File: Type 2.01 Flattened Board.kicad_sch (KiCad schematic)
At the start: 8 parts, among them U10 74AHC125

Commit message: Redo pinout to simplify routing
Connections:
- net BUS.PA2: no longer XA2.A0
- net BUS.PA4: no longer XA2.D2 (D2_INT0)
- net BUS.PA5: no longer XA2.A1
- net BUS.PA6: no longer XA2.D3 (D3_INT1)
- net BUS.PA7: no longer XA2.D4
- net BUS.PB3: no longer XA2.A2
- net BUS.PB4: no longer XA2.A3
- net BUS.PB5: no longer XA2.A4
- net BUS.PB6: no longer XA2.A5
- net BUS.PB7: no longer XA2.D5
- net BUS.PB8: no longer XA2.D6
- net BUS.PB9: no longer XA2.D7
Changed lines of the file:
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@@
     (company "Joshua Scoggins")
   )
+  (bus_alias "CCL" (members "IN[0..11]" "OUT[0..3]"))
   (bus_alias "MetroM4" (members "D[0..13]" "SCL" "SDA" "AREF" "A[0..5]" "MISO" "MOSI" "SCK" "~{RESET[0..1]}" "VIN"))
-  (bus_alias "CCL" (members "IN[0..11]" "OUT[0..3]"))
   (junction (at 54.102 162.052) (diameter 0) (color 0 0 0 0)
   )
@@
     (stroke (width 0) (type default) (color 0 0 0 0))
   )
+  (bus_entry (at 251.46 86.36) (size 2.54 2.54)
+    (stroke (width 0) (type default) (color 0 0 0 0))
+  )
+  (bus_entry (at 248.92 86.36) (size 2.54 2.54)
+    (stroke (width 0) (type default) (color 0 0 0 0))
+  )
   (bus_entry (at 23.368 141.732) (size 2.54 2.54)
     (stroke (width 0) (type default) (color 0 0 0 0))
@@
     (stroke (width 0) (type default) (color 0 0 0 0))
   )
+  (bus (pts (xy 248.92 86.36) (xy 251.46 86.36))
+    (stroke (width 0) (type default) (color 0 0 0 0))
+  )
   (wire (pts (xy 312.039 38.1) (xy 347.345 38.1))
     (stroke (width 0) (type default) (color 0 0 0 0))
@@
     (stroke (width 0) (type default) (color 0 0 0 0))
   )
-  (bus (pts (xy 246.38 86.36) (xy 309.499 86.36))
+  (bus (pts (xy 246.38 86.36) (xy 248.92 86.36))
     (stroke (width 0) (type default) (color 0 0 0 0))
   )
@@
     (stroke (width 0) (type default) (color 0 0 0 0))
   )
+  (bus (pts (xy 251.46 86.36) (xy 309.499 86.36))
+    (stroke (width 0) (type default) (color 0 0 0 0))
+  )
   (wire (pts (xy 139.7 108.712) (xy 187.452 108.712))
     (stroke (width 0) (type default) (color 0 0 0 0))
@@
     (stroke (width 0) (type default) (color 0 0 0 0))
   )
+  (wire (pts (xy 254 88.9) (xy 254 102.87))
+    (stroke (width 0) (type default) (color 0 0 0 0))
+  )
   (wire (pts (xy 256.54 184.785) (xy 271.145 184.785))
     (stroke (width 0) (type default) (color 0 0 0 0))
@@
   )
   (bus (pts (xy 238.76 86.36) (xy 241.3 86.36))
+    (stroke (width 0) (type default) (color 0 0 0 0))
+  )
+  (wire (pts (xy 251.46 88.9) (xy 251.46 102.87))
     (stroke (width 0) (type default) (color 0 0 0 0))
   )
@@
     (effects (font (size 1.27 1.27)) (justify right bottom))
   )
-  (label "BUS.PC18" (at 347.345 73.66 180)
+  (label "BUS.PC18" (at 359.41 90.17 180)
     (effects (font (size 1.27 1.27)) (justify right bottom))
   )
@@
     (effects (font (size 1.27 1.27)) (justify left bottom))
   )
-  (label "BUS.PB8" (at 189.484 226.822 180)
+  (label "BUS.PB8" (at 347.345 76.2 180)
     (effects (font (size 1.27 1.27)) (justify right bottom))
   )
@@
     (effects (font (size 1.27 1.27)) (justify left bottom))
   )
-  (label "BUS.PB4" (at 34.544 239.522 0)
-    (effects (font (size 1.27 1.27)) (justify left bottom))
+  (label "BUS.PB4" (at 347.345 68.58 180)
+    (effects (font (size 1.27 1.27)) (justify right bottom))
   )
   (label "BUS.PC15" (at 145.288 154.432 0)
     (effects (font (size 1.27 1.27)) (justify left bottom))
   )
-  (label "BUS.PA4" (at 189.484 216.662 180)
+  (label "BUS.PA4" (at 347.345 73.66 180)
     (effects (font (size 1.27 1.27)) (justify right bottom))
   )
@@
     (effects (font (size 1.27 1.27)) (justify right bottom))
   )
-  (label "BUS.PD21" (at 347.345 86.36 180)
+  (label "BUS.PD21" (at 384.81 70.485 180)
     (effects (font (size 1.27 1.27)) (justify right bottom))
   )
@@
     (effects (font (size 1.27 1.27)) (justify right bottom))
   )
-  (label "BUS.PB23" (at 347.345 66.04 180)
+  (label "BUS.PB23" (at 365.76 74.93 180)
     (effects (font (size 1.27 1.27)) (justify right bottom))
   )
@@
     (effects (font (size 1.27 1.27)) (justify right bottom))
   )
-  (label "BUS.PC21" (at 347.345 81.28 180)
+  (label "BUS.PC21" (at 389.89 86.36 180)
     (effects (font (size 1.27 1.27)) (justify right bottom))
   )
@@
     (effects (font (size 1.27 1.27)) (justify left bottom))
   )
-  (label "BUS.PB22" (at 347.345 63.5 180)
+  (label "BUS.PB22" (at 381.635 57.15 180)
     (effects (font (size 1.27 1.27)) (justify right bottom))
   )
@@
     (effects (font (size 1.27 1.27)) (justify left bottom))
   )
-  (label "BUS.PB2" (at 347.345 68.58 180)
-    (effects (font (size 1.27 1.27)) (justify right bottom))
-  )
-  (label "BUS.PA2" (at 34.544 247.142 0)
-    (effects (font (size 1.27 1.27)) (justify left bottom))
+  (label "BUS.PB2" (at 359.41 85.09 180)
+    (effects (font (size 1.27 1.27)) (justify right bottom))
+  )
+  (label "BUS.PA2" (at 251.46 89.535 270)
+    (effects (font (size 1.27 1.27)) (justify right bottom))
   )
   (label "GCM4.D11" (at 312.547 134.62 0)
@@
     (effects (font (size 1.27 1.27)) (justify left bottom))
   )
-  (label "BUS.PB3" (at 34.544 242.062 0)
-    (effects (font (size 1.27 1.27)) (justify left bottom))
+  (label "BUS.PB3" (at 347.345 86.36 180)
+    (effects (font (size 1.27 1.27)) (justify right bottom))
   )
   (label "~{RESET_{0}}" (at 189.484 267.462 180)
     (effects (font (size 1.27 1.27)) (justify right bottom))
   )
-  (label "BUS.PA6" (at 189.484 219.202 180)
+  (label "BUS.PA6" (at 347.345 81.28 180)
     (effects (font (size 1.27 1.27)) (justify right bottom))
   )
@@
     (effects (font (size 1.27 1.27)) (justify left bottom))
   )
-  (label "BUS.PB6" (at 34.544 234.442 0)
-    (effects (font (size 1.27 1.27)) (justify left bottom))
+  (label "BUS.PB6" (at 347.345 63.5 180)
+    (effects (font (size 1.27 1.27)) (justify right bottom))
   )
   (label "SPI_MOSI" (at 102.87 42.164 270)
@@
     (effects (font (size 1.27 1.27)) (justify left bottom))
   )
-  (label "BUS.PD20" (at 347.345 83.82 180)
+  (label "BUS.PD20" (at 384.81 67.945 180)
     (effects (font (size 1.27 1.27)) (justify right bottom))
   )
@@
     (effects (font (size 1.27 1.27)) (justify left bottom))
   )
-  (label "BUS.PB7" (at 189.484 224.282 180)
+  (label "BUS.PB7" (at 347.345 66.04 180)
     (effects (font (size 1.27 1.27)) (justify right bottom))
   )
@@
     (effects (font (size 1.27 1.27)) (justify left bottom))
   )
-  (label "BUS.PA7" (at 189.484 221.742 180)
+  (label "BUS.PA7" (at 347.345 83.82 180)
     (effects (font (size 1.27 1.27)) (justify right bottom))
   )
@@
     (effects (font (size 1.27 1.27)) (justify right bottom))
   )
+  (label "GCM4.~{BE1}" (at 254 102.87 270)
+    (effects (font (size 1.27 1.27)) (justify right bottom))
+  )
   (label "BUS.PA7" (at 61.214 144.272 0)
     (effects (font (size 1.27 1.27)) (justify left bottom))
@@
     (effects (font (size 1.27 1.27)) (justify left bottom))
   )
-  (label "BUS.PB5" (at 34.544 236.982 0)
-    (effects (font (size 1.27 1.27)) (justify left bottom))
+  (label "BUS.PB5" (at 347.345 71.12 180)
+    (effects (font (size 1.27 1.27)) (justify right bottom))
   )
   (label "GCM4.D7" (at 312.547 124.46 0)
     (effects (font (size 1.27 1.27)) (justify left bottom))
   )
-  (label "BUS.PB18" (at 347.345 71.12 180)
+  (label "BUS.PB18" (at 375.285 86.995 180)
     (effects (font (size 1.27 1.27)) (justify right bottom))
   )
@@
     (effects (font (size 1.27 1.27)) (justify left bottom))
   )
-  (label "BUS.PB9" (at 189.484 229.362 180)
+  (label "BUS.PB9" (at 347.345 78.74 180)
     (effects (font (size 1.27 1.27)) (justify right bottom))
   )
@@
     (effects (font (size 1.27 1.27)) (justify right bottom))
   )
-  (label "BUS.PC19" (at 347.345 76.2 180)
+  (label "BUS.PC19" (at 384.175 79.375 180)
     (effects (font (size 1.27 1.27)) (justify right bottom))
   )
@@
     (effects (font (size 1.27 1.27)) (justify left bottom))
   )
-  (label "BUS.PA5" (at 34.544 244.602 0)
-    (effects (font (size 1.27 1.27)) (justify left bottom))
+  (label "BUS.PA5" (at 254 89.535 270)
+    (effects (font (size 1.27 1.27)) (justify right bottom))
   )
   (label "BUS.PC17" (at 347.345 129.54 180)
     (effects (font (size 1.27 1.27)) (justify right bottom))
   )
-  (label "BUS.PC20" (at 347.345 78.74 180)
-    (effects (font (size 1.27 1.27)) (justify right bottom))
-  )
+  (label "GCM4.~{BE0}" (at 251.46 102.87 270)
+    (effects (font (size 1.27 1.27)) (justify right bottom))
+  )
+  (label "BUS.PC20" (at 363.855 80.01 180)
+    (effects (font (size 1.27 1.27)) (justify right bottom))
+  )

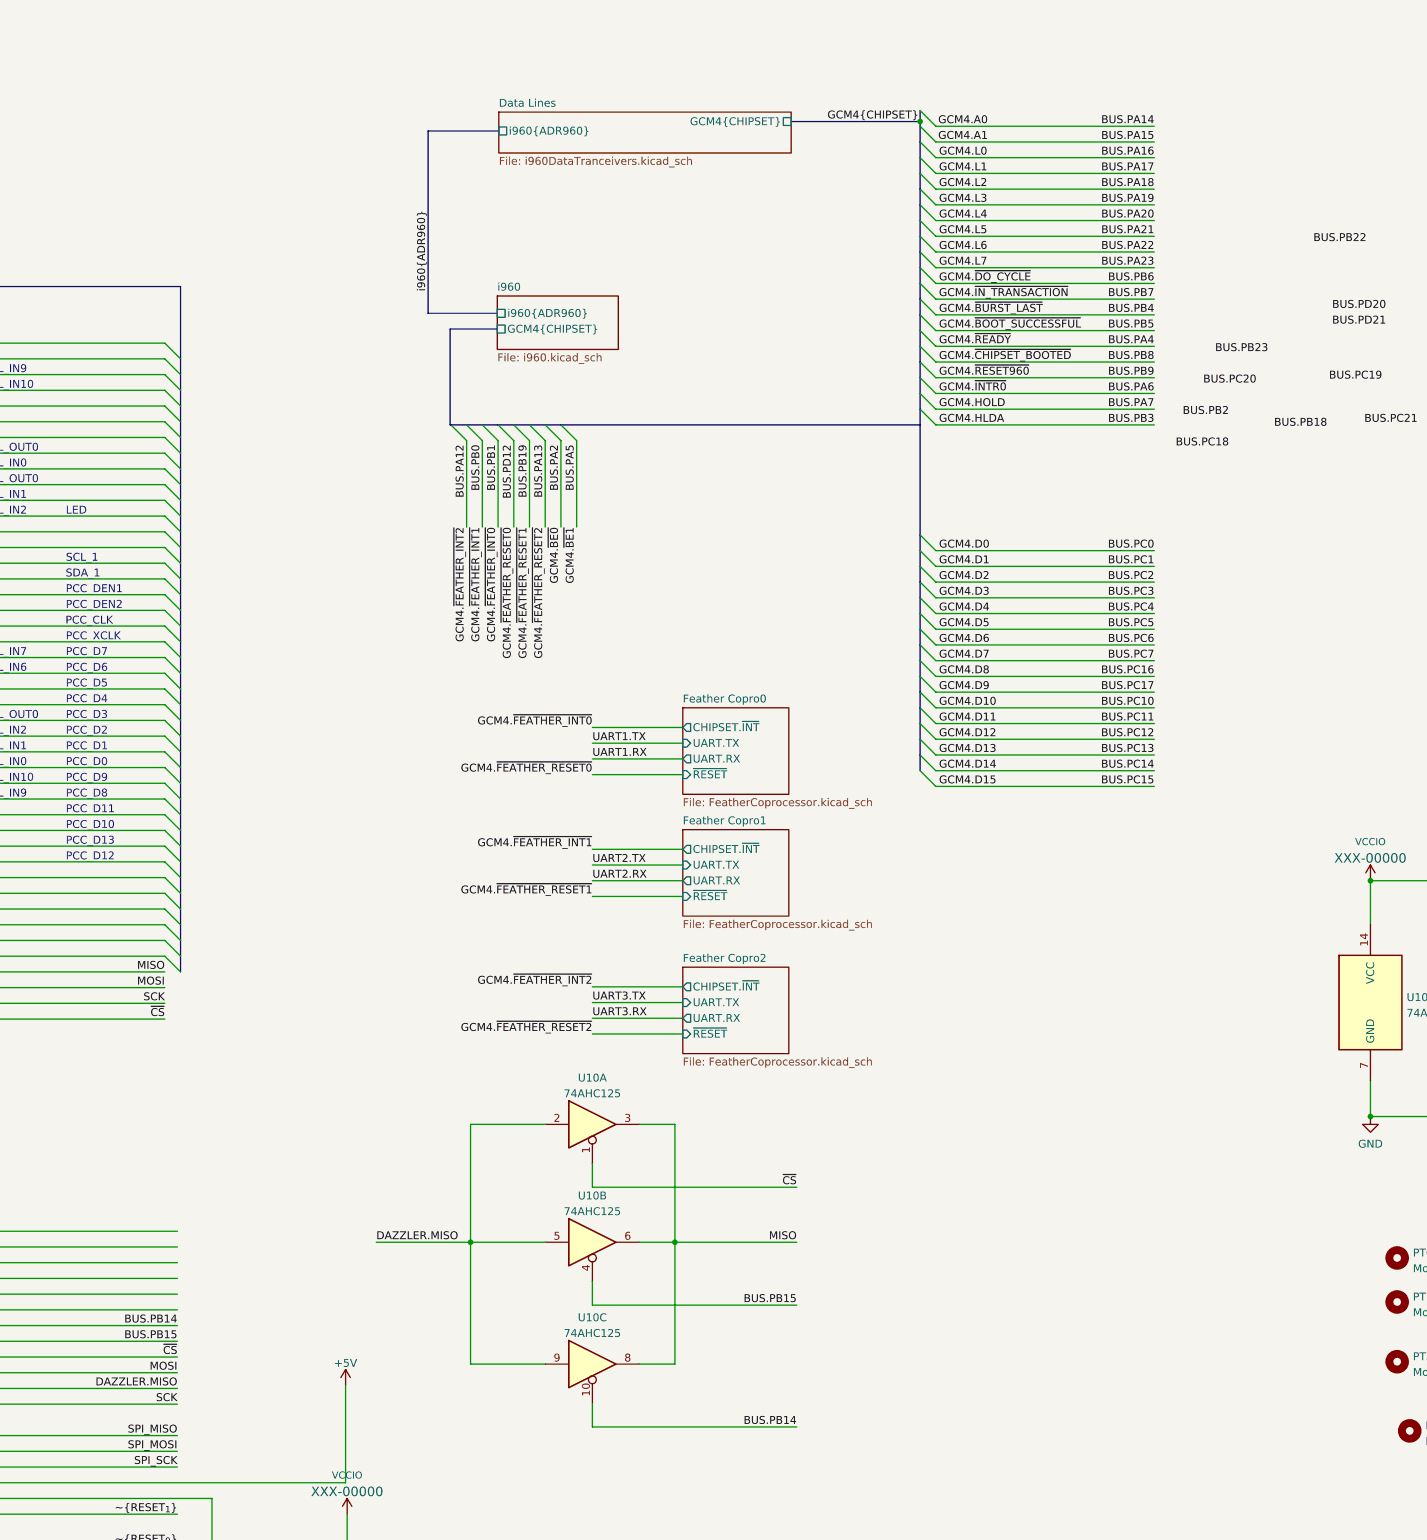
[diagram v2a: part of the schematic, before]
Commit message: Drop the number of feather co processors down to 1
The dazzler provides audio and video so the only thing left would be
around bluetooth or something similar
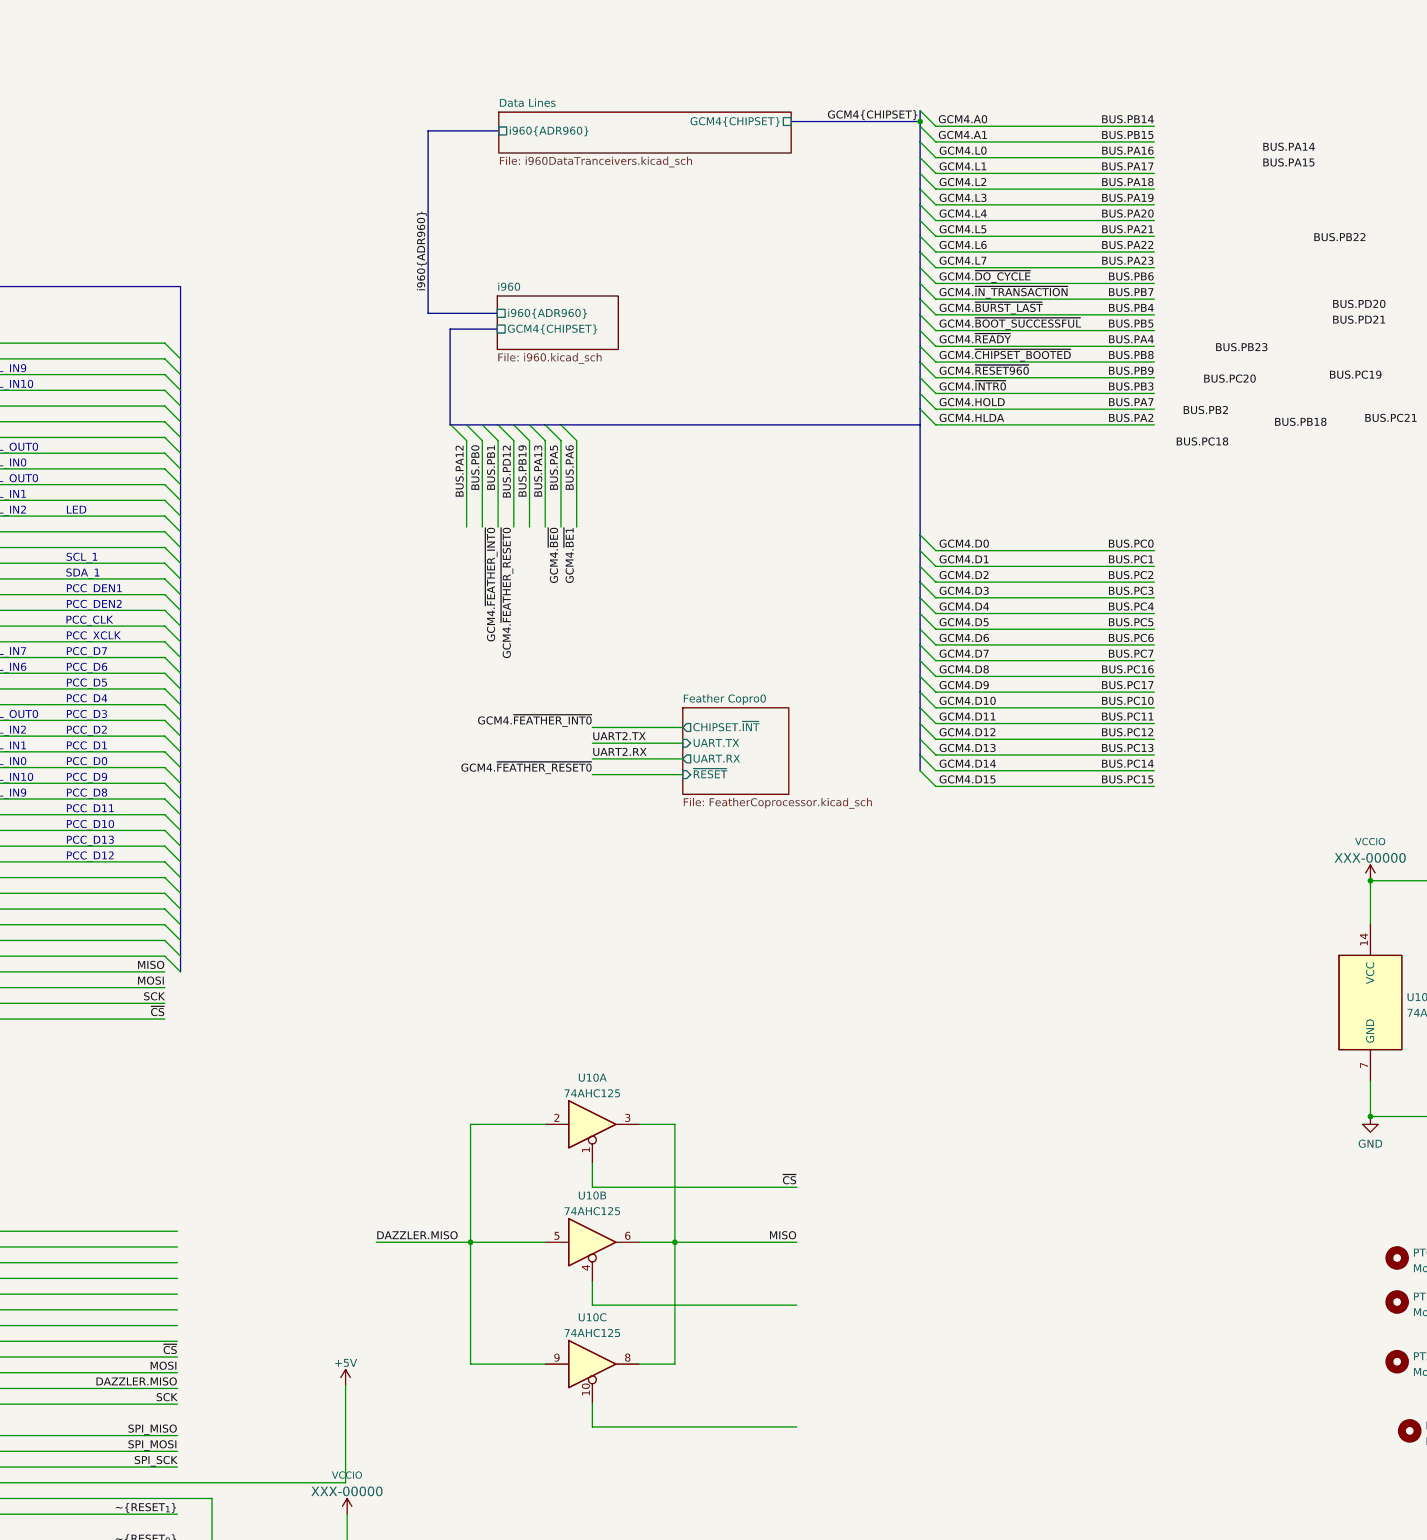
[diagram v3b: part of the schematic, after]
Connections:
- net BUS.PB14: no longer U10.10, XA2.D8
- net BUS.PB15: no longer U10.4, XA2.D9
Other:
- removed sheet Feather Copro1
- removed sheet Feather Copro2

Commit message: do proper pin layouts for inputs from the i960
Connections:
- net BUS.PA2: now also XA2.A0
- net BUS.PA5: now also XA2.A1
- net BUS.PB18: now also XA2.D8
- net BUS.PB2: now also XA2.D9
- net BUS.PB3: now also XA2.A2
- net BUS.PC18: now also XA2.D2 (D2_INT0)
- net BUS.PC19: now also XA2.D3 (D3_INT1)
- net BUS.PC20: now also XA2.D4
- net BUS.PC21: now also XA2.D5
- net BUS.PD20: now also XA2.D6
- net BUS.PD21: now also XA2.D7
- net UART1.RX renamed BUS.PB13
- net UART1.TX renamed BUS.PB12
- net UART2.RX renamed BUS.PC23
- net UART2.TX renamed BUS.PC22
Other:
- note added: "UART1.RX"
- note added: "UART1.TX"
- note added: "UART2.RX"
- note added: "UART2.TX"
- note removed: "BUS.PB12"
- note removed: "BUS.PB13"
- note removed: "BUS.PC22"
- note removed: "BUS.PC23"
- moved on the sheet: XA2
